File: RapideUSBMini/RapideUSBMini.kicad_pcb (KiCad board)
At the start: 2 copper layers, 50.5 x 40 mm, 14 parts, among them J2 AVR-ISP-6, U1 ATtiny85-20P, Y1 12MHz

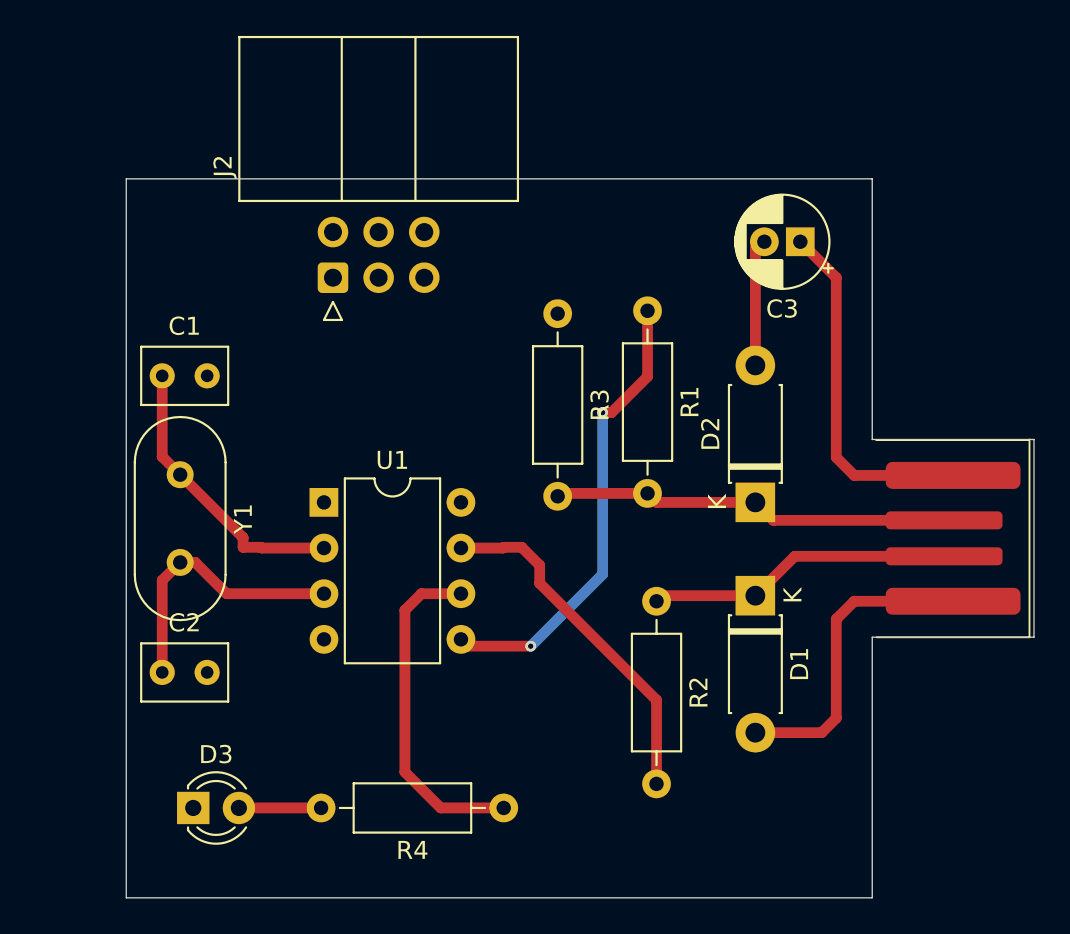
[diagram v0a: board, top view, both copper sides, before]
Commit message: PCB nearly ok for home production, now tuning
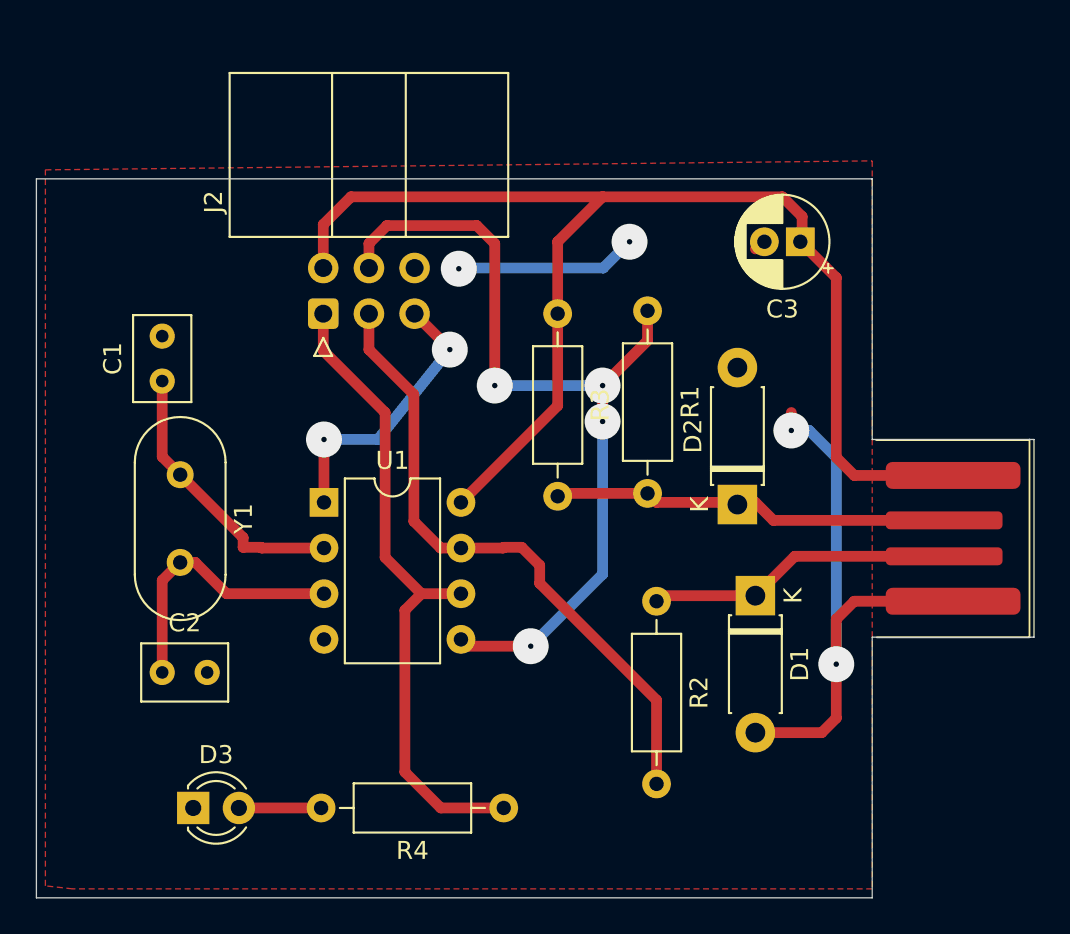
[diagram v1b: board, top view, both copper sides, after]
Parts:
- moved J2 2.07 mm to (151.0, 67.5)
- moved D2 1.01 mm to (174.0, 78.1)
- moved C1 0.29 mm to (142.0, 71.2), turned to 90 degrees
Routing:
- net +5V: track 19.7 -> 71.5 mm
- net /MOSI: track 25.7 -> 50.0 mm, vias 2 -> 4
- net GND: track 24.3 -> 44.1 mm, vias 0 -> 4
- net /MISO: track 18.8 -> 36.7 mm
- net /SCK: track 19.7 -> 35.5 mm
- net /RST: track 0.00 -> 15.7 mm, vias 0 -> 2
- added copper zone on F.Cu, net GND
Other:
- board size 50.5 x 40 mm -> 55.5 x 40 mm
